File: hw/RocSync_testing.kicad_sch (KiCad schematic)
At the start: 37 parts, among them J1 USB_C_Receptacle_PowerOnly_6P, J2 BATT, J3 PROG, SW1 ON/OFF, SW2 RESET, SW3 MODE, U1 BQ24075RGT, U16 MT3608, U2 CH32V003FxUx, Y1 Crystal_GND24

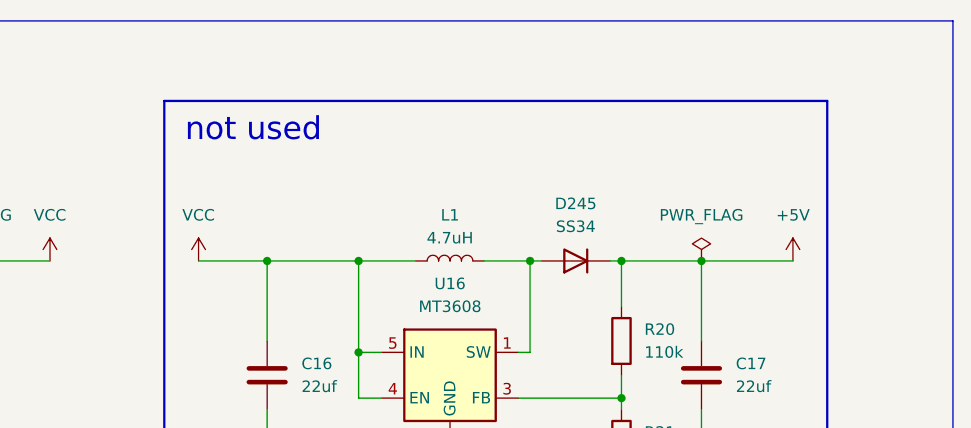
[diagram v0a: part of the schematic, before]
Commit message: schematics: add note about step-up regulator
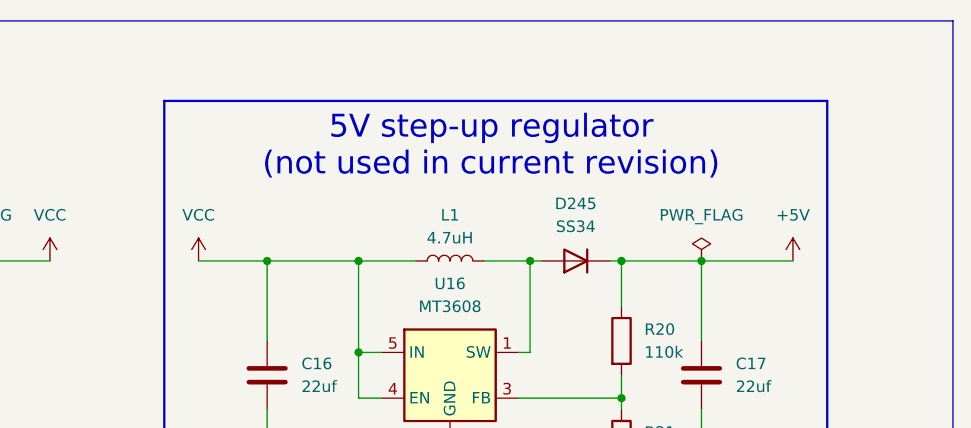
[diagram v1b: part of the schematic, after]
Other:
- note added: "5V step-up regulator (not used in current revision)"
- note removed: "not used"
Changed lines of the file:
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@@
 		)
 	)
-	(text "not used"
+	(text "5V step-up regulator\n(not used in current revision)"
 		(exclude_from_sim no)
-		(at 205.486 26.162 0)
+		(at 231.902 27.94 0)
 		(effects
 			(font

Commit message: [hw] rev 2
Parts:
- removed C5, C6: 10pf, Capacitor_SMD:C_0402_1005Metric, symbol Device:C
- removed JP1: CHG BOOST, Jumper:SolderJumper-2_P1.3mm_Open_RoundedPad1.0x1.5mm, symbol Jumper:SolderJumper_2_Open
- removed Y1: Crystal_GND24, Crystal:Crystal_SMD_2520-4Pin_2.5x2.0mm, symbol Device:Crystal_GND24
- added C16, C7: 1uf, Capacitor_SMD:C_0402_1005Metric, symbol Device:C
- added C17: 10nF, Capacitor_SMD:C_0402_1005Metric, symbol Device:C
- added C19: 0.1uf, Capacitor_SMD:C_0402_1005Metric, symbol Device:C
- added J4: Conn_01x04_Socket, Connector_PinHeader_2.54mm:PinHeader_1x04_P2.54mm_Vertical, symbol Connector:Conn_01x04_Socket
- added R21: 5.1k, Resistor_SMD:R_0402_1005Metric, symbol Device:R
- added R22: 1.8k, Resistor_SMD:R_0402_1005Metric, symbol Device:R
- added R24: 510, Resistor_SMD:R_0402_1005Metric, symbol Device:R
- added R26: 10k, Resistor_SMD:R_0402_1005Metric, symbol Device:R
- added R27: 2k, Resistor_SMD:R_0402_1005Metric, symbol Device:R
- added SW4, SW5, SW6, SW7: SW_Push, custom_footprints:SW_Push_1P1T_NO_6x6mm_H9.5mm, symbol Switch:SW_Push
- added U16: TPS7A2025, Package_TO_SOT_SMD:SOT-23-5, symbol Regulator_Linear:TPS76325
- added Y1: huaxindianzi 2T024000VX, Oscillator:Oscillator_SMD_SeikoEpson_TG2520SMN-xxx-xxxxxx-4Pin_2.5x2.0mm, symbol custom_symbols:huaxindianzi_2T024000VX
- C18: value 0.1uf -> 10pF
- C20: renamed from C16; now not fitted
- C21: renamed from C17; now not fitted
- D278: renamed from D245; now not fitted
- J3: value PROG -> Conn_01x03_Pin
- L1: now not fitted
- R23: value 1.18k -> 820
- R28: renamed from R20; now not fitted
- R29: renamed from R21; now not fitted
- R3: renamed from R22; value 1.18k -> 1.1k
- R4: renamed from R3; value 2k -> 590
- SW2: footprint Button_Switch_SMD:SW_Push_1P1T_NO_6x6mm_H9.5mm -> custom_footprints:SW_Push_1P1T_NO_6x6mm_H9.5mm
- SW3: value MODE -> SW_Push; footprint Button_Switch_SMD:SW_Push_1P1T_NO_6x6mm_H9.5mm -> custom_footprints:SW_Push_1P1T_NO_6x6mm_H9.5mm; now in the parts list
- U17: renamed from U16; now not fitted
- renumbered C3 to C2, C2 to C3, C7 to C5, D241 to D275, D242 to D276, D243 to D277, R6 to R19, R19 to R20, R4 to R5, R5 to R6
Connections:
- net +BATT: now also J2.1 (Pin_1); no longer J2.2 (Pin_2)
- net GND: now also J2.2 (Pin_2), SW3.2, C16.2, C17.2, C19.2, C7.2, J4.1 (Pin_1), R26.2, SW4.2, SW5.2, SW6.2, SW7.2, U16.2 (GND), Y1.1 (NC/GND), Y1.2 (GND); no longer J2.1 (Pin_1), SW3.1
- net OSCI: now also C18.1, R26.1, Y1.3 (OUT)
- net RING_LATCH: now also U2.11 (PC4); no longer U2.8 (PC1)
- net VCC: now also C7.1, J4.2 (Pin_2), R27.2, U16.1 (VIN), U16.3 (EN)
- net at R23.1: now also R22.2, SW5.1
- net at R4.2, U1.16 (ISET): no longer R23.2
- net OSCO renamed BTN_LADDER
- net BTN_LADDER: now also C19.1, R24.2, R27.1, SW7.1
- new net: R21.1, SW3.1
- new net: R23.2, R24.1, SW6.1
- new net: R21.2, R22.1, SW4.1
- new net: C16.1, C17.1, U16.5 (VOUT), Y1.4 (Vdd)
- new net SCL: J4.3 (Pin_3), U2.9 (PC2)
- new net SDA: J4.4 (Pin_4), U2.8 (PC1)
- no-connect marks 7 -> 6
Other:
- sheet Counter LEDs: file untitled.kicad_sch -> counter.kicad_sch
- sheet Ring LEDs 1-16: file untitled.kicad_sch -> ring_segment.kicad_sch
- sheet Ring LEDs 17-32: file untitled.kicad_sch -> ring_segment.kicad_sch
- sheet Ring LEDs 33-48: file untitled.kicad_sch -> ring_segment.kicad_sch
- sheet Ring LEDs 49-64: file untitled.kicad_sch -> ring_segment.kicad_sch
- sheet Ring LEDs 65-80: file untitled.kicad_sch -> ring_segment.kicad_sch
- sheet Ring LEDs 81-96: file untitled.kicad_sch -> ring_segment.kicad_sch
- sheet Ring LEDs 97-100: file 4leds.kicad_sch -> ring_segment_small.kicad_sch
- note added: "5-Way Joystick"
- note added: "Clock"
- note added: "USB input current: 1550 AΩ / 1.1 kΩ = 1.4 A Battery charging current: 890 AΩ / 590 kΩ = 1.5 A"
- note removed: "USB input current: 1550 AΩ / 1.18 kΩ = 1.31 A Battery charging current (default): 890 AΩ / 2 kΩ = 0.445 A Battery charging current (boost): 890 AΩ / 742 Ω = 1.2 A"
- moved on the sheet: C4, C5, D277, J3, R20, R3, SW2, U2
